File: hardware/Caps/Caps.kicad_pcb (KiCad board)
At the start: 2 copper layers, 75 x 42 mm, 116 parts

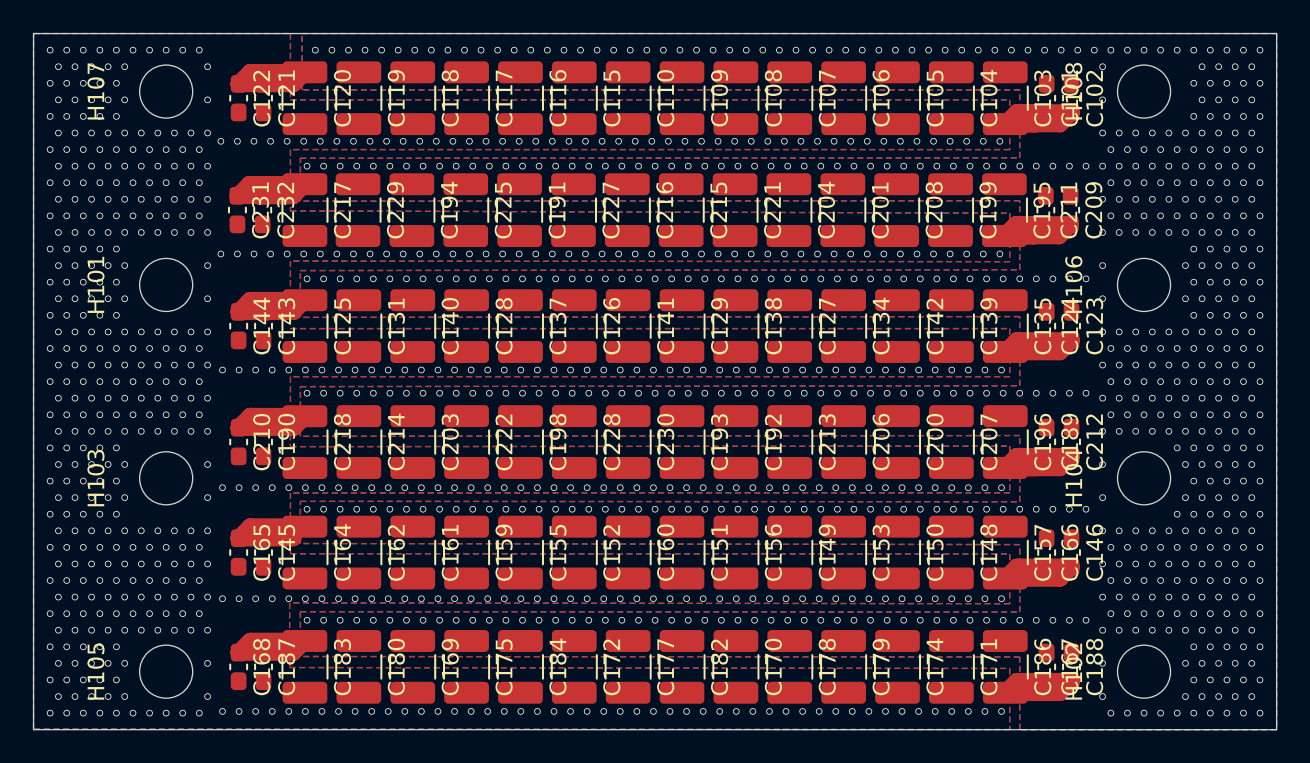
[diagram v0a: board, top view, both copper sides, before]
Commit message: A lot of clarance issues fixed, gerbers added
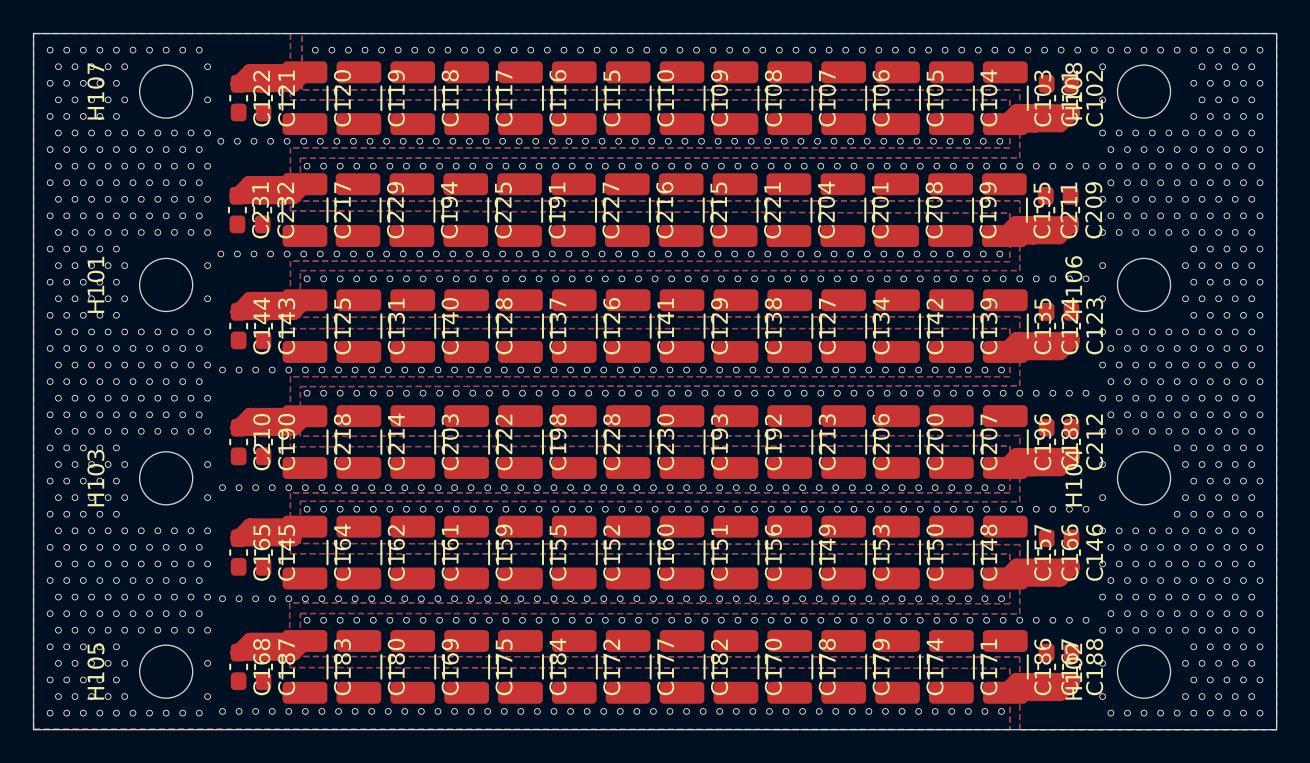
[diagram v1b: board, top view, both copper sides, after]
